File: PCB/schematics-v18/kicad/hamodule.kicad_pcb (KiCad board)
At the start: 2 copper layers, 78.4 x 84.3 mm, 100 parts, among them J1 Conn_01x02_Male, J10 2604-1104, J11 ESP Relays, J12 2604-1104, J13 EspSense, J2 2604-1102, J3 GND|5V, J4 GND|3.3V, J5 Jumper, J6 Conn_01x02_Male, J7 Current Jumper, J8 USB_C_Receptacle_USB2.0, J9 DoNotCon, K1 PCN-105D, K2 PCN-105D, K3 PCN-105D, K4 PCN-105D, Q1 SS8050-SMD, Q2 SS8050, SW1 EN, SW2 IO0, U1 LD1117AV33_TO220, U2 ESP32-WROOM-32E, U3 CP2102N-A01-GQFN28, U4 ULN2003A, U5 LDA210-PDIP, U6 LDA210-PDIP, U7 SHT4x

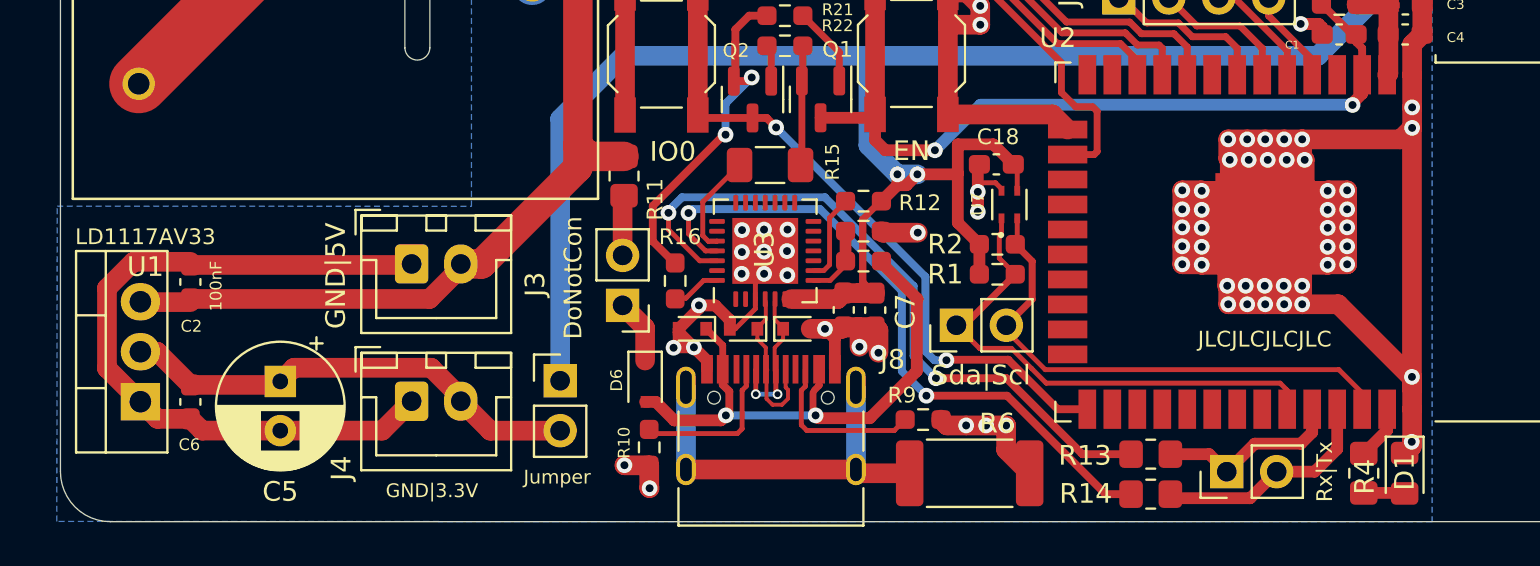
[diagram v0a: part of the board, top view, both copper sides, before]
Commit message: digikey + moving LDA up + small trace route
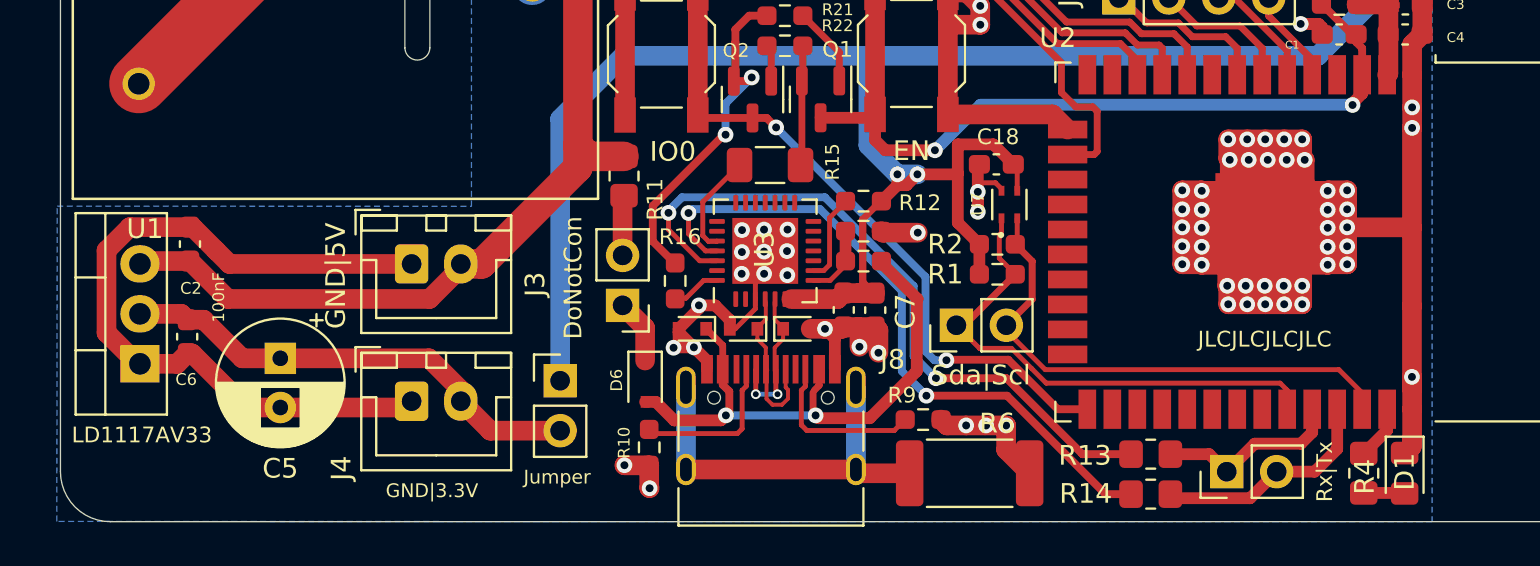
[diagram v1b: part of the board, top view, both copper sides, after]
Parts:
- moved C6 3.32 mm to (131.6, 142.3)
- moved U1 1.93 mm to (129.2, 143.7)
- moved C2 1.93 mm to (131.7, 137.6)
- moved C5 1.18 mm to (136.3, 143.4)
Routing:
- net GND: track 302.4 -> 293.8 mm, vias 82 -> 81
- net 5V+: track 98.8 -> 99.7 mm

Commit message: minor changes
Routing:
- net D+: track 8.32 -> 10.5 mm
- net VBUS: track 29.1 -> 30.5 mm
- net GND: track 293.8 -> 294.6 mm, vias 81 -> 61

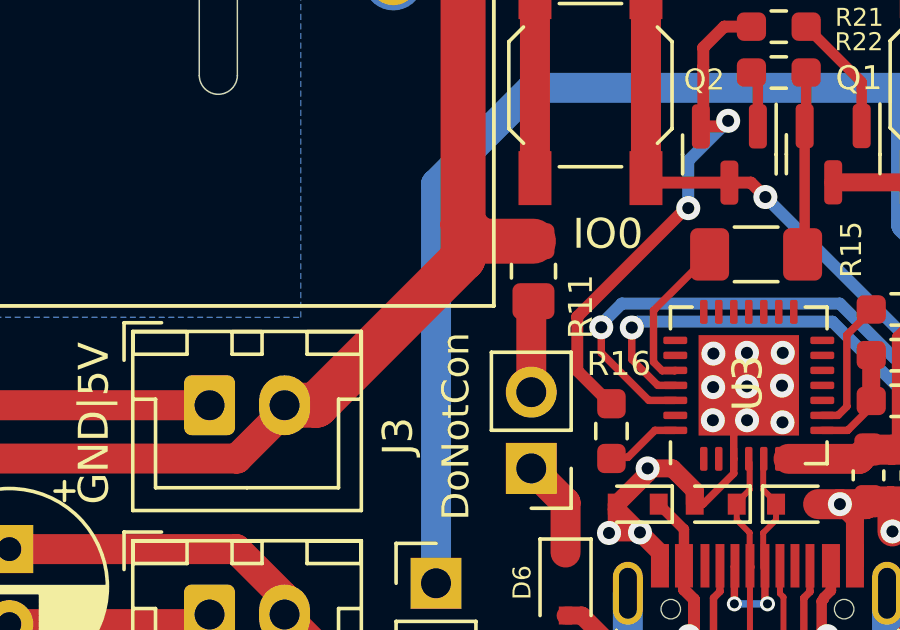
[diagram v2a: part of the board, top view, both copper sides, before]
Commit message: removing useless USB resistor
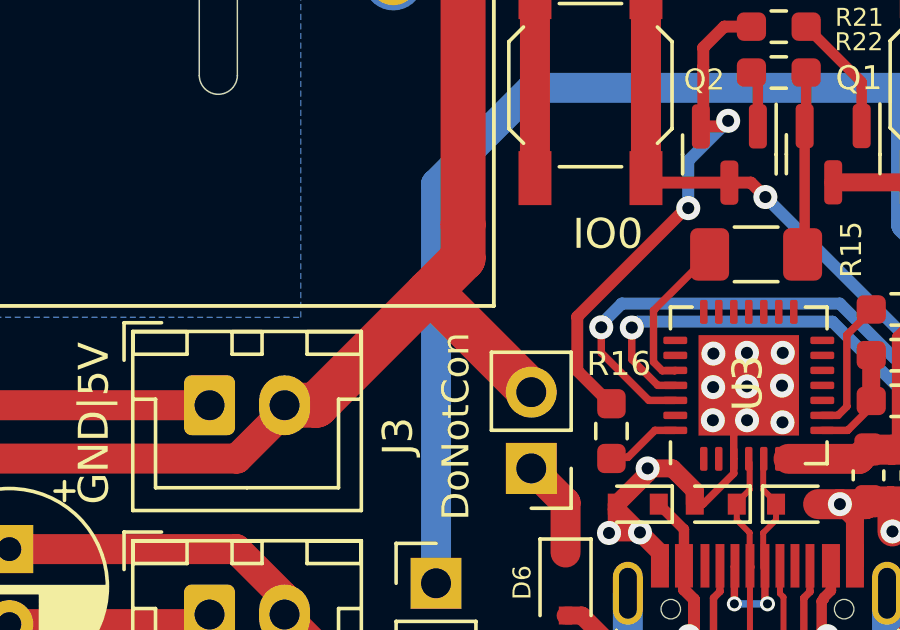
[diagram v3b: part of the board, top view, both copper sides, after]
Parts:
- removed R11: 50Ω, Resistor_SMD:R_0805_2012Metric_Pad1.20x1.40mm_HandSolder
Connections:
- J9 pad 2: Net-(J9-Pad2) -> 5V+
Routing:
- net Net-(J9-Pad2): track 3.06 -> 0.00 mm
- net 5V+: track 99.7 -> 101.9 mm

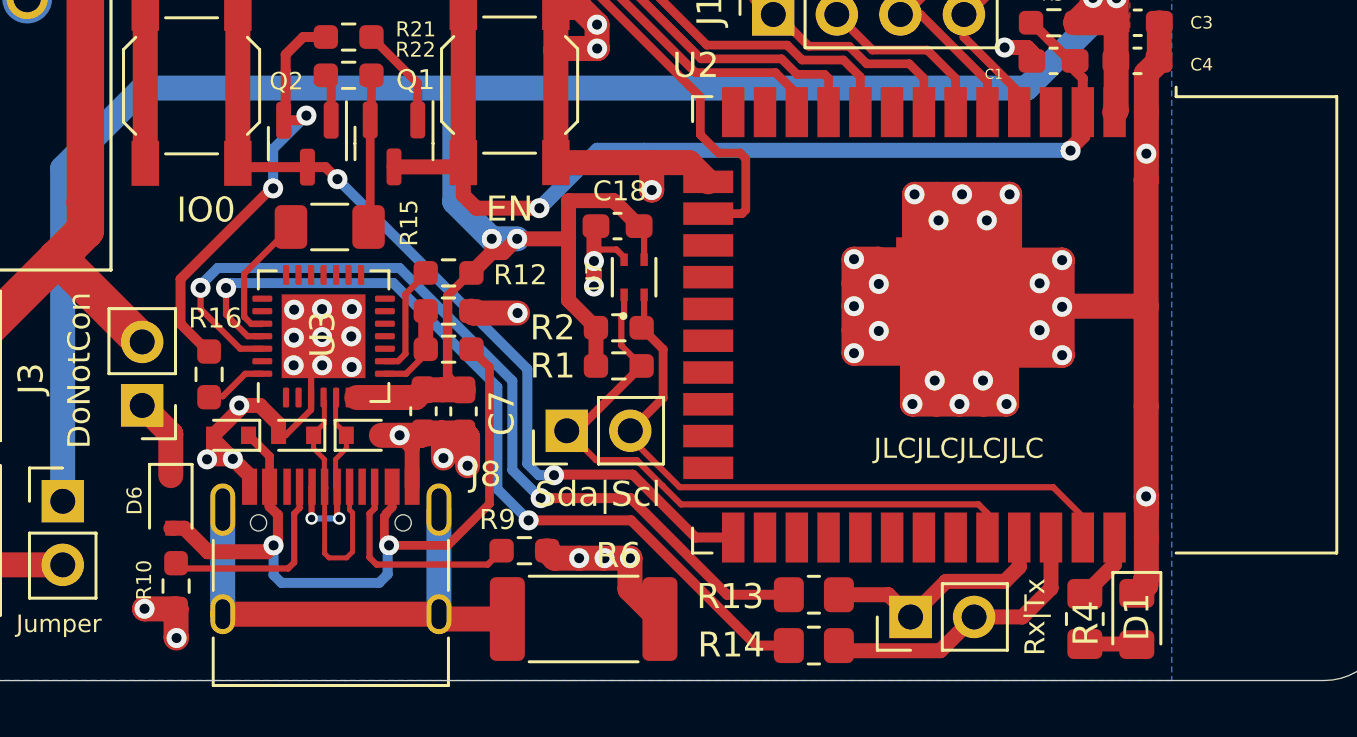
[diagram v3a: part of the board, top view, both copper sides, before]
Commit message: flipping SHT40 and adding bigger pads for easier soldering
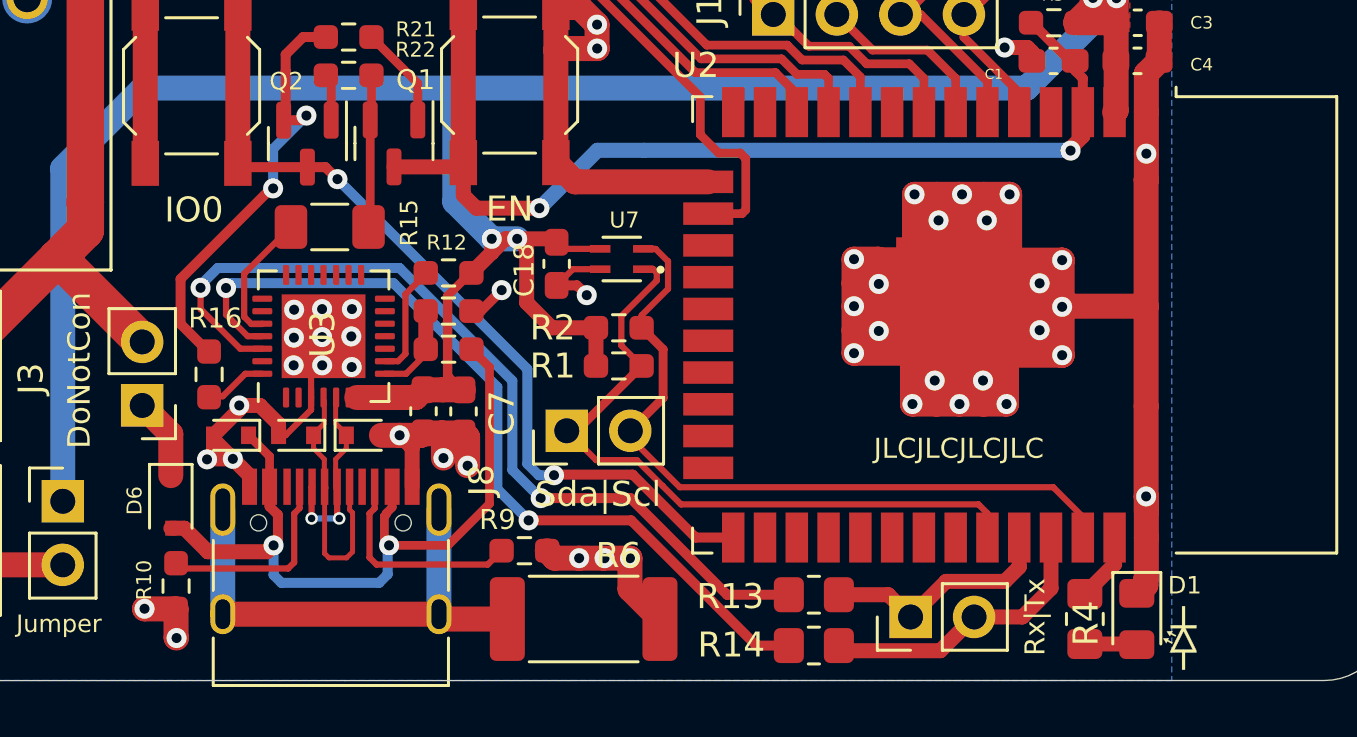
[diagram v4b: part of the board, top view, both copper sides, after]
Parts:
- added G2: LOGO, icons:led_6000dpi, F.Cu at (195.2, 150.0)
- moved C18 2.86 mm to (170.3, 135.0), turned to -90 degrees
- moved U7 0.88 mm to (172.9, 134.9), turned to 180 degrees
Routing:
- net GND: track 294.6 -> 291.5 mm, vias 61 -> 59
- net SCL: track 32.0 -> 34.9 mm
- net 3.3V+: track 139.8 -> 137.0 mm
- net SDA: track 26.4 -> 28.5 mm

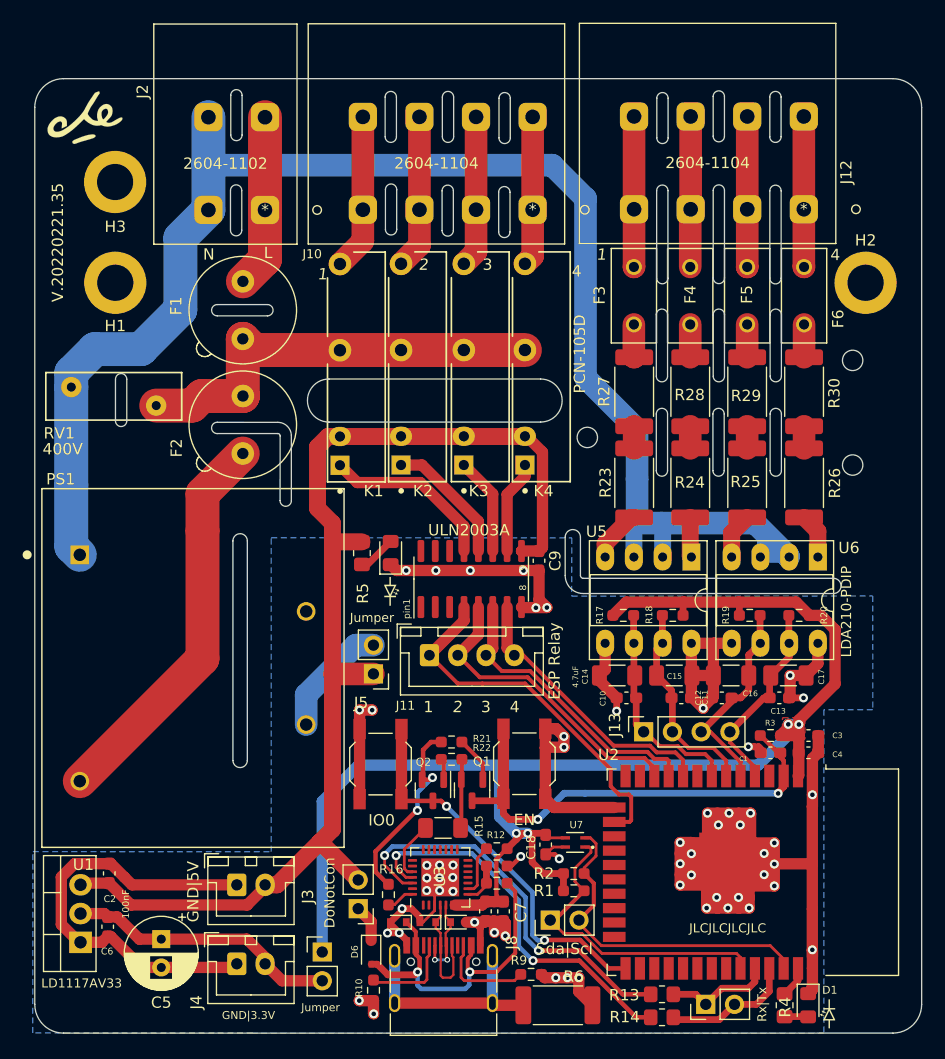
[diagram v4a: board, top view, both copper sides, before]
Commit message: adding fuses for output + 3d modules for wago
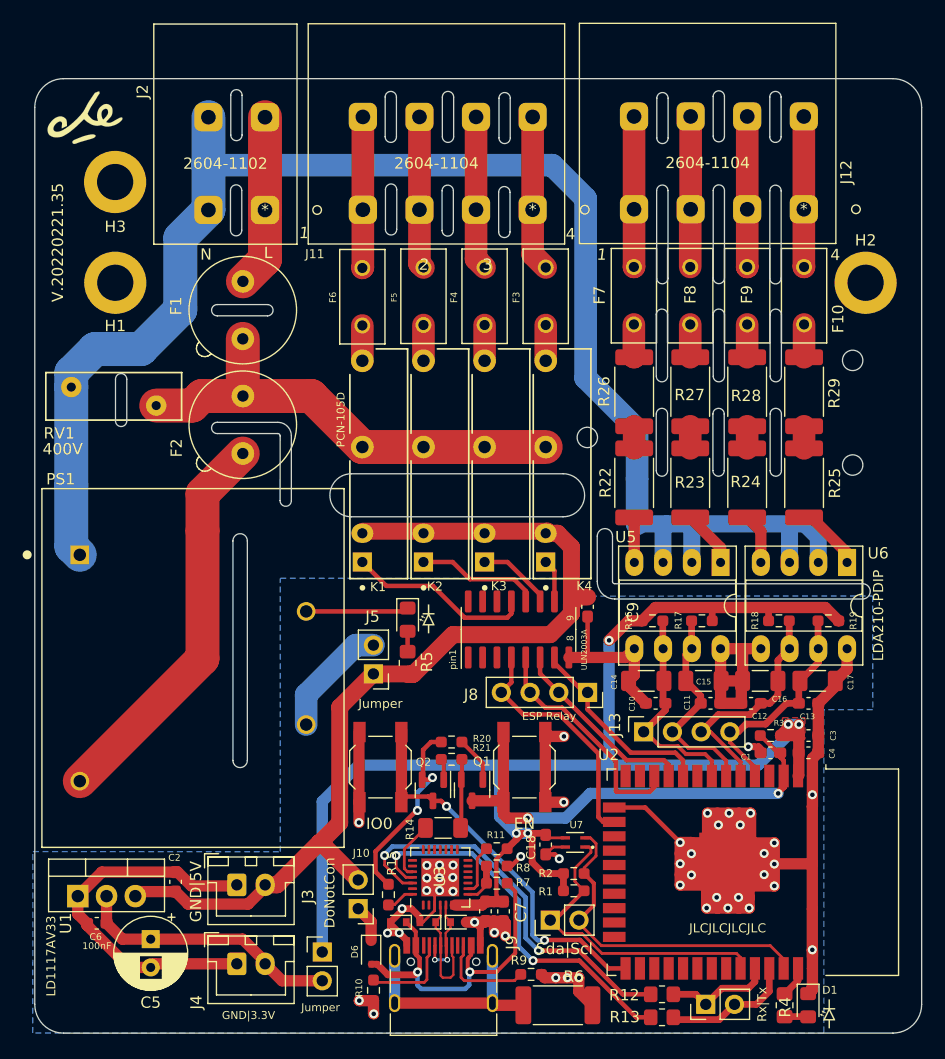
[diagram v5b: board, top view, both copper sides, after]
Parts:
- removed G4: LOGO, icons:depsi
- removed the J11 at (160.0, 118.3)
- added F3: Fuse, RST-80-AMMO:FUSE_RST-1-BULK, F.Cu at (170.3, 86.6)
- added F4: Fuse, RST-80-AMMO:FUSE_RST-1-BULK, F.Cu at (164.9, 86.6)
- added F5: Fuse, RST-80-AMMO:FUSE_RST-1-BULK, F.Cu at (159.5, 86.6)
- added F6: Fuse, RST-80-AMMO:FUSE_RST-1-BULK, F.Cu at (154.1, 86.6)
- added G***: LOGO, icons:depsi, B.Cu at (192.2, 138.3)
- added J8: EspRelays, Connector_PinSocket_2.54mm:PinSocket_1x04_P2.54mm_Vertical, F.Cu at (174.0, 121.6)
- SW1: value EN -> Switch
- SW2: value IO0 -> Switch
- moved R5 10.5 mm to (158.1, 119.0), turned to -90 degrees
- moved K2 8.79 mm to (160.9, 101.4)
- moved K1 8.78 mm to (155.6, 101.4)
- moved K4 8.76 mm to (171.8, 101.4)
- moved K3 8.76 mm to (166.3, 101.4)
- moved U4 6.11 mm to (167.9, 116.0)
- moved D2 6.07 mm to (158.1, 115.2), turned to -90 degrees
- moved C9 5.91 mm to (174.0, 114.0)
- moved C2 5.91 mm to (137.6, 138.3)
- moved U1 4.09 mm to (129.0, 139.6), turned to 0 degrees
- moved G2 3.93 mm to (159.8, 115.1), turned to 90 degrees
- moved C10 2.62 mm to (180.0, 122.6)
- moved C14 2.62 mm to (179.2, 120.6)
- moved U6 2.62 mm to (196.9, 110.1)
- moved C11 2.62 mm to (184.9, 122.6)
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- renumbered F6 to F10, F3 to F7, F4 to F8, F5 to F9, J9 to J10, J10 to J11, J8 to J9, R12 to R11, R13 to R12, R14 to R13, R15 to R14, R16 to R15, R17 to R16, R18 to R17, R19 to R18, R20 to R19, R21 to R20, R22 to R21, R23 to R22, R24 to R23, R25 to R24, R26 to R25, R27 to R26, R28 to R27, R29 to R28, R30 to R29
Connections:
- J11 pad 1: REO4 -> Net-(F3-Pad2)
- J11 pad 2: REO4 -> Net-(F3-Pad2)
- J11 pad 3: REO3 -> Net-(F4-Pad2)
- J11 pad 4: REO3 -> Net-(F4-Pad2)
- J11 pad 5: REO2 -> Net-(F5-Pad2)
- J11 pad 6: REO2 -> Net-(F5-Pad2)
- J11 pad 7: REO1 -> Net-(F6-Pad2)
- J11 pad 8: REO1 -> Net-(F6-Pad2)
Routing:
- net Net-(F3-Pad2): track 0.00 -> 13.8 mm
- net Net-(F4-Pad2): track 0.00 -> 13.6 mm
- net Net-(F5-Pad2): track 0.00 -> 13.5 mm
- net Net-(F6-Pad2): track 0.00 -> 13.4 mm
- net EspRel1: track 33.0 -> 21.5 mm
- net REO1: track 13.8 -> 3.12 mm
- net REO2: track 13.7 -> 3.16 mm
- net REO3: track 13.4 -> 3.16 mm
- net REO4: track 13.3 -> 3.16 mm
- net EspRel3: track 25.9 -> 17.1 mm
- net 5V+: track 101.9 -> 93.6 mm
- net GND: track 291.5 -> 284.5 mm, vias 59 -> 48
- net EspRel4: track 24.7 -> 17.7 mm
- net EspRel2: track 27.2 -> 20.5 mm
- net REI4: track 8.25 -> 3.80 mm
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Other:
- outline, holes or cut-outs redrawn
